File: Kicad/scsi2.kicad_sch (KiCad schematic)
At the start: 30 parts, among them J3 TO-LED, J4 TO-MB, J8 TO-A3000-LED, J9 TO-A3000-MB, U10 NCR53c710 SCSI Host Controller, U13 SST39SF010/020/040, Y1 Abracon ACO-50MHz

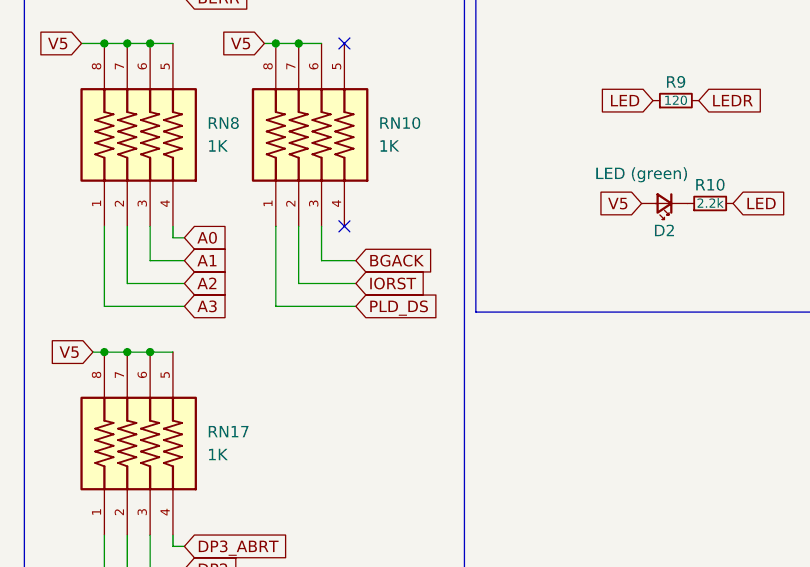
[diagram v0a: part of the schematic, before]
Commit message: Kicad: Pin swaps on RN10 and RN16
Fixes issue #1 and issue #2
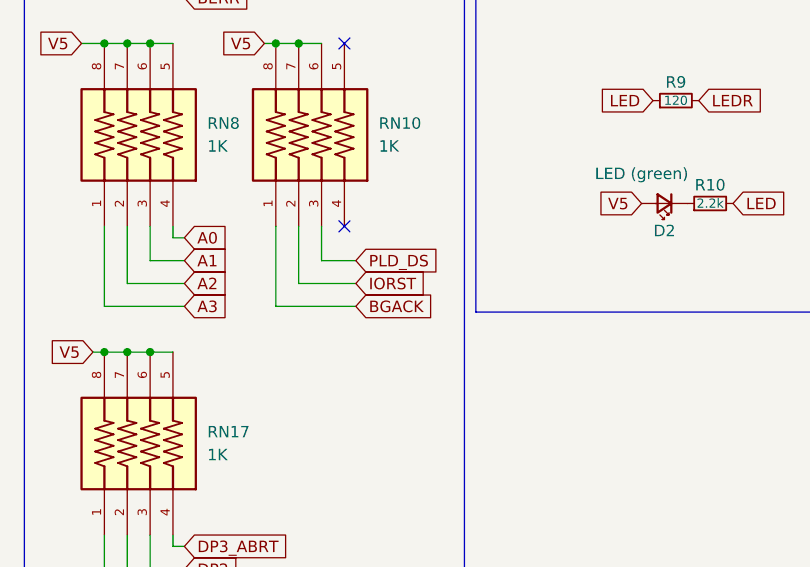
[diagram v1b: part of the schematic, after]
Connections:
- net BGACK: now also RN10.1; no longer RN10.3
- net PLD_DS: now also RN10.3; no longer RN10.1
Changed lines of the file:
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@@
 		)
 	)
+	(global_label "BGACK"
+		(shape input)
+		(at 152.4 157.48 0)
+		(fields_autoplaced yes)
+		(effects
+			(font
+				(size 1.27 1.27)
+			)
+			(justify left)
+		)
+		(property "Intersheetrefs" "${INTERSHEET_REFS}"
+			(at 161.5538 157.48 0)
+			(effects
+				(font
+					(size 1.27 1.27)
+				)
+				(justify left)
+				(hide yes)
+			)
+		)
+	)
 	(global_label "PLD_SIZ1"
 		(shape input)
@@
 		)
 	)
-	(global_label "BGACK"
-		(shape input)
-		(at 152.4 152.4 0)
-		(fields_autoplaced yes)
-		(effects
-			(font
-				(size 1.27 1.27)
-			)
-			(justify left)
-		)
-		(property "Intersheetrefs" "${INTERSHEET_REFS}"
-			(at 161.5538 152.4 0)
-			(effects
-				(font
-					(size 1.27 1.27)
-				)
-				(justify left)
-				(hide yes)
-			)
-		)
-	)
 	(global_label "A22"
 		(shape input)
@@
 		)
 	)
+	(global_label "PLD_DS"
+		(shape input)
+		(at 152.4 152.4 0)
+		(fields_autoplaced yes)
+		(effects
+			(font
+				(size 1.27 1.27)
+			)
+			(justify left)
+		)
+		(property "Intersheetrefs" "${INTERSHEET_REFS}"
+			(at 162.4004 152.4 0)
+			(effects
+				(font
+					(size 1.27 1.27)
+				)
+				(justify left)
+				(hide yes)
+			)
+		)
+	)
 	(global_label "A1"
 		(shape input)
@@
 			(effects
 				(font
-					(size 1.27 1.27)
-				)
-				(justify left)
-				(hide yes)
-			)
-		)
-	)
-	(global_label "PLD_DS"
-		(shape input)
-		(at 152.4 157.48 0)
-		(fields_autoplaced yes)
-		(effects
-			(font
-				(size 1.27 1.27)
-			)
-			(justify left)
-		)
-		(property "Intersheetrefs" "${INTERSHEET_REFS}"
-			(at 162.4004 157.48 0)
-			(effects
-				(font
